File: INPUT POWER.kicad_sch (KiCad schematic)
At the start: 5 parts, among them J1 TYPE-C-31-M12_13

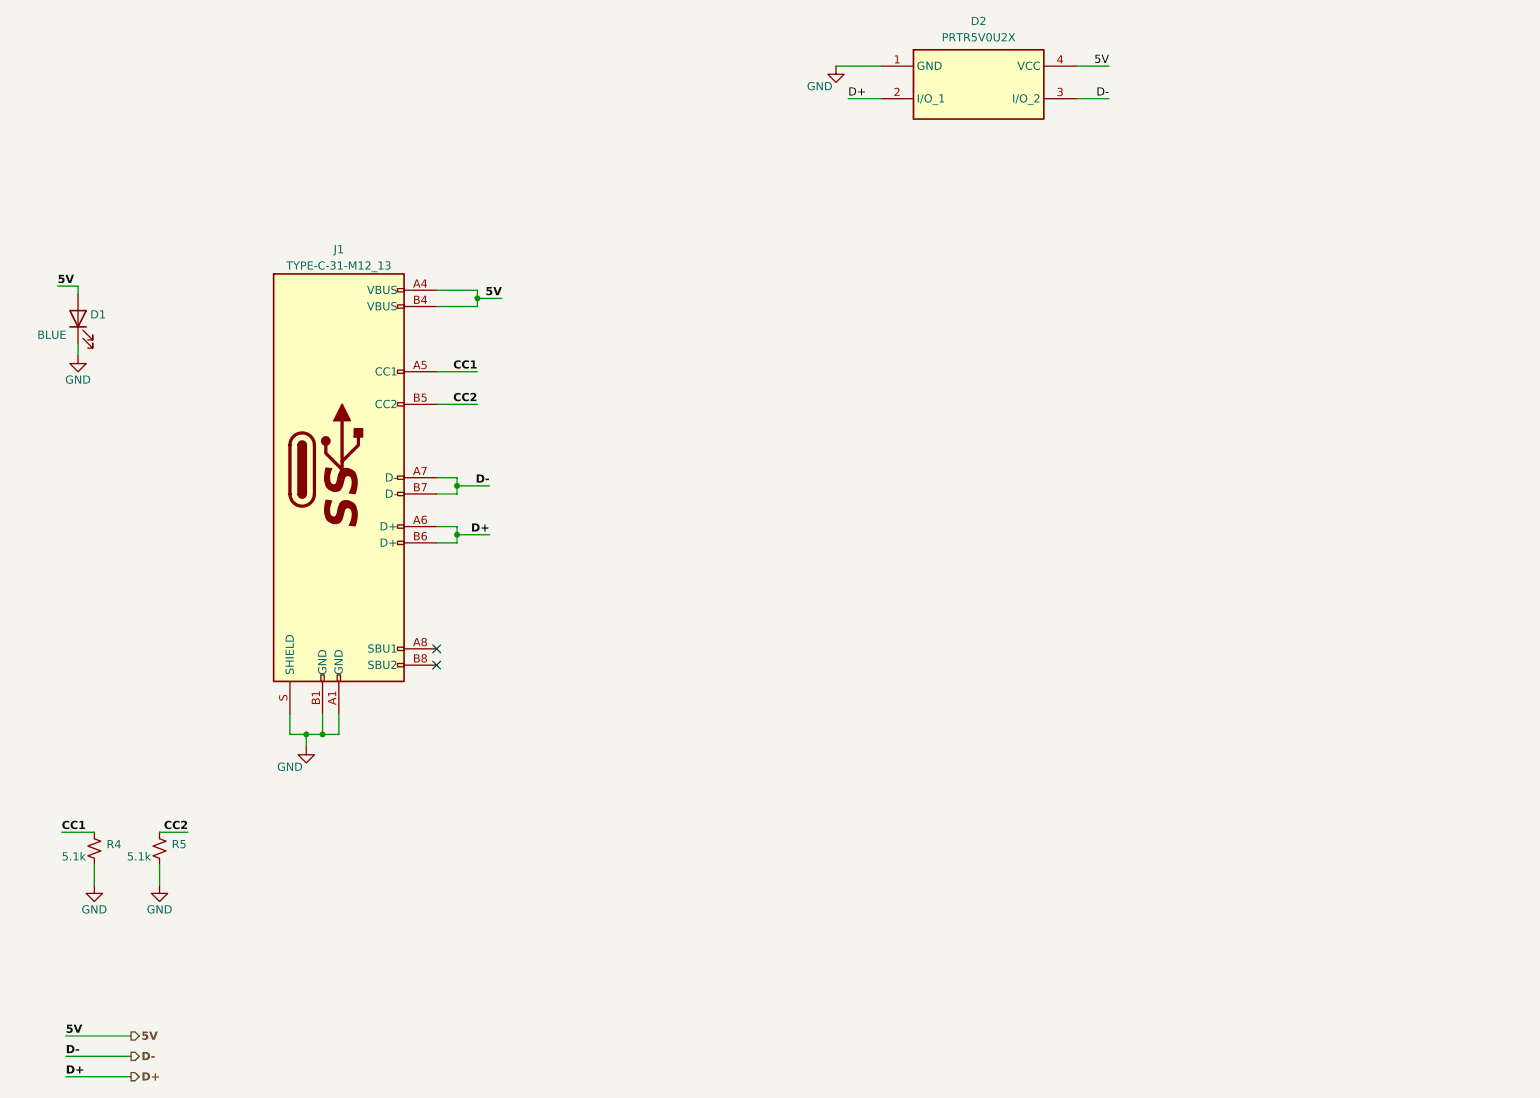
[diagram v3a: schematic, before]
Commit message: Added IP5306 for power path management
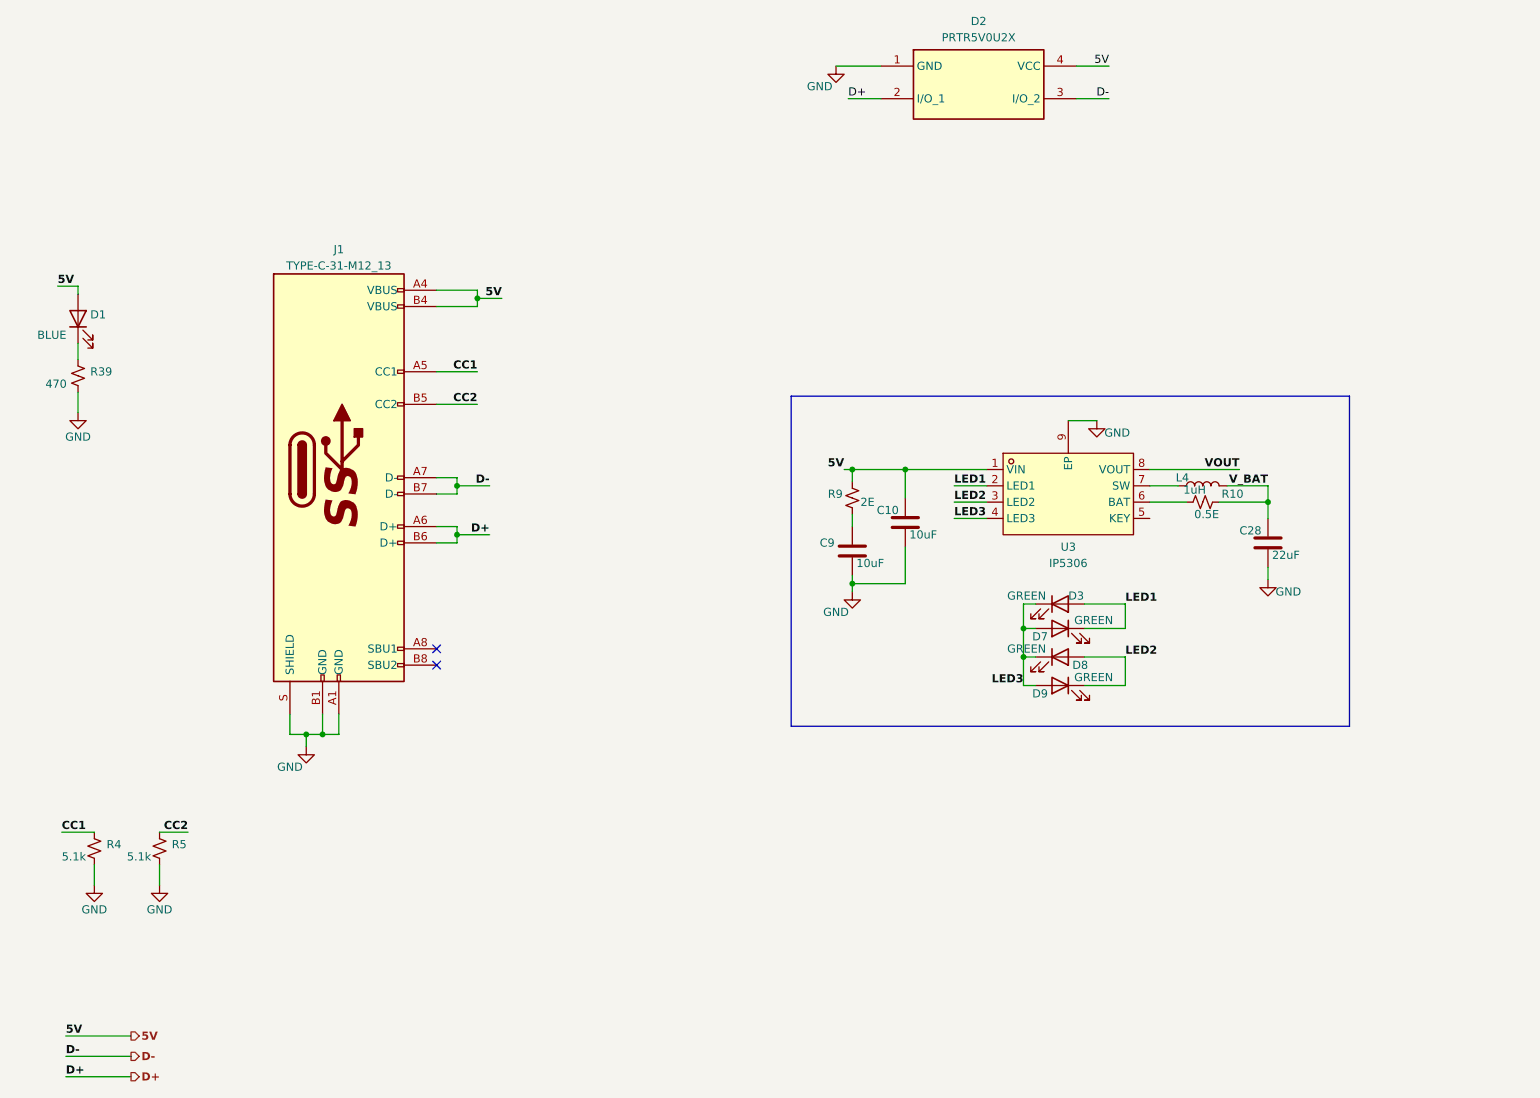
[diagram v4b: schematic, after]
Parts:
- added C10, C9: 10uF, symbol ESP32-S3_DB:C
- added C28: 22uF, symbol ESP32-S3_DB:C
- added D3, D7, D8, D9: GREEN, symbol ESP32-S3_DB:LED
- added L4: 1uH, symbol ESP32-S3_DB:L
- added R10: 0.5E, symbol ESP32-S3_DB:R_Small_US
- added R39: 470, symbol ESP32-S3_DB:R_Small_US
- added R9: 2E, symbol ESP32-S3_DB:R_Small_US
- added U3: IP5306, easyeda2kicad:ESOP-8_L4.9-W3.9-P1.27-LS6.0-BL-EP, symbol ESP32-S3_DB:IP5306
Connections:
- net 5V: now also C10.1, R9.1, U3.1 (VIN)
- net GND: now also C10.2, C28.2, C9.2, R39.2, U3.9 (EP); no longer D1.1 (K)
- new net: C9.1, R9.2
- new net: D1.1 (K), R39.1
- new net: R10.1, U3.6 (BAT)
- new net: L4.1, U3.7 (SW)
- new net LED1: D3.2 (A), D7.1 (K), U3.2 (LED1)
- new net LED2: D8.2 (A), D9.1 (K), U3.3 (LED2)
- new net LED3: D3.1 (K), D7.2 (A), D8.1 (K), D9.2 (A), U3.4 (LED3)
- new net VOUT: U3.8 (VOUT)
- new net V_BAT: C28.1, L4.2, R10.2

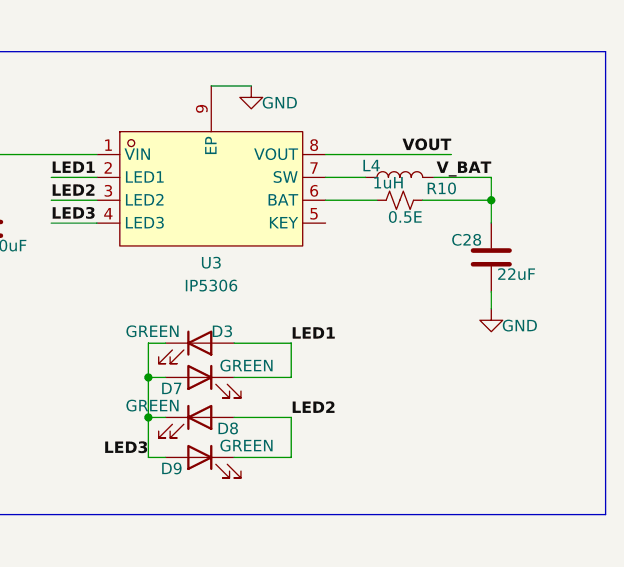
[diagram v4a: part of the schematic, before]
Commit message: Assigned UART port 2 for RS-485
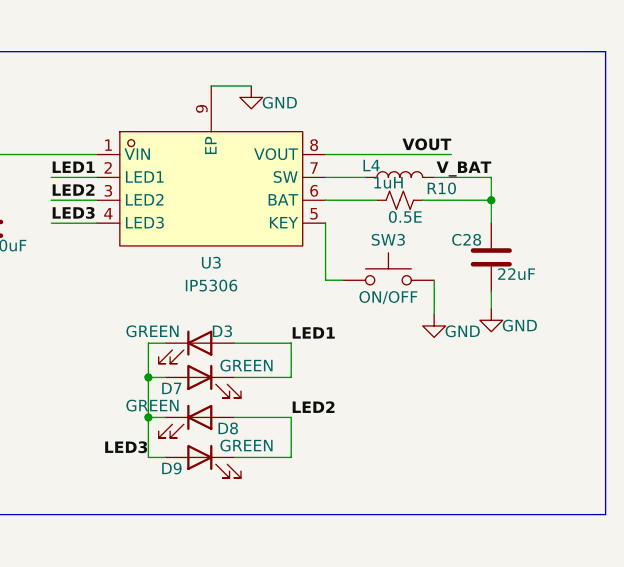
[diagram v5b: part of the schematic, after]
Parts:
- added SW3: ON/OFF, symbol ESP32-S3_DB:SW_Push
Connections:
- net GND: now also SW3.2
- net at U3.5 (KEY): now also SW3.1
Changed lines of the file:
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@@
+    (stroke (width 0) (type default))
+  )
+  (wire (pts (xy 205.105 111.76) (xy 205.105 107.95))
     (stroke (width 0) (type default))
   )
@@
   )
   (wire (pts (xy 173.355 114.935) (xy 173.355 118.745))
+    (stroke (width 0) (type default))
+  )
+  (wire (pts (xy 193.04 107.95) (xy 194.945 107.95))
     (stroke (width 0) (type default))
   )
@@
   )
   (wire (pts (xy 26.035 85.09) (xy 26.035 81.915))
+    (stroke (width 0) (type default))
+  )
+  (wire (pts (xy 193.04 101.6) (xy 193.04 107.95))
     (stroke (width 0) (type default))
   )
@@
         (path "/b7fc4bd3-c219-4455-832b-8d795385dcf1/95090a63-7b3c-4ea0-92b8-aeafe05264cd"
           (reference "R39") (unit 1)
+        )
+      )
+    )
+  )
+  (symbol (lib_id "ESP32-S3_DB:GND") (at 205.105 111.76 0) (unit 1)
+    (in_bom yes) (on_board yes) (dnp no)
+    (property "Reference" "#PWR053" (at 205.105 118.11 0)
+      (effects (font (size 1.27 1.27)) hide)
+    )
+    (property "Value" "GND" (at 208.28 113.665 0)
+      (effects (font (size 1.27 1.27)))
+    )
+    (property "Footprint" "" (at 205.105 111.76 0)
+      (effects (font (size 1.27 1.27)) hide)
+    )
+    (property "Datasheet" "" (at 205.105 111.76 0)
+      (effects (font (size 1.27 1.27)) hide)
+    )
+    (pin "1")
+    (instances
+      (project "ESP32-S3_DB"
+        (path "/b7fc4bd3-c219-4455-832b-8d795385dcf1/95090a63-7b3c-4ea0-92b8-aeafe05264cd"
+          (reference "#PWR053") (unit 1)
         )
       )
@@
         )
       )
+    )
+  )
+  (symbol (lib_id "ESP32-S3_DB:SW_Push") (at 200.025 107.95 0) (unit 1)
+    (in_bom yes) (on_board yes) (dnp no)
+    (property "Reference" "SW3" (at 200.025 103.505 0)
+      (effects (font (size 1.27 1.27)))
+    )
+    (property "Value" "ON/OFF" (at 200.025 109.855 0)
+      (effects (font (size 1.27 1.27)))
+    )
+    (property "Footprint" "" (at 200.025 102.87 0)
+      (effects (font (size 1.27 1.27)) hide)
+    )
+    (property "Datasheet" "~" (at 200.025 102.87 0)
+      (effects (font (size 1.27 1.27)) hide)
+    )
+    (pin "1")
+    (pin "2")
+    (instances
+      (project "ESP32-S3_DB"
+        (path "/b7fc4bd3-c219-4455-832b-8d795385dcf1/95090a63-7b3c-4ea0-92b8-aeafe05264cd"
+          (reference "SW3") (unit 1)
+        )
+      )

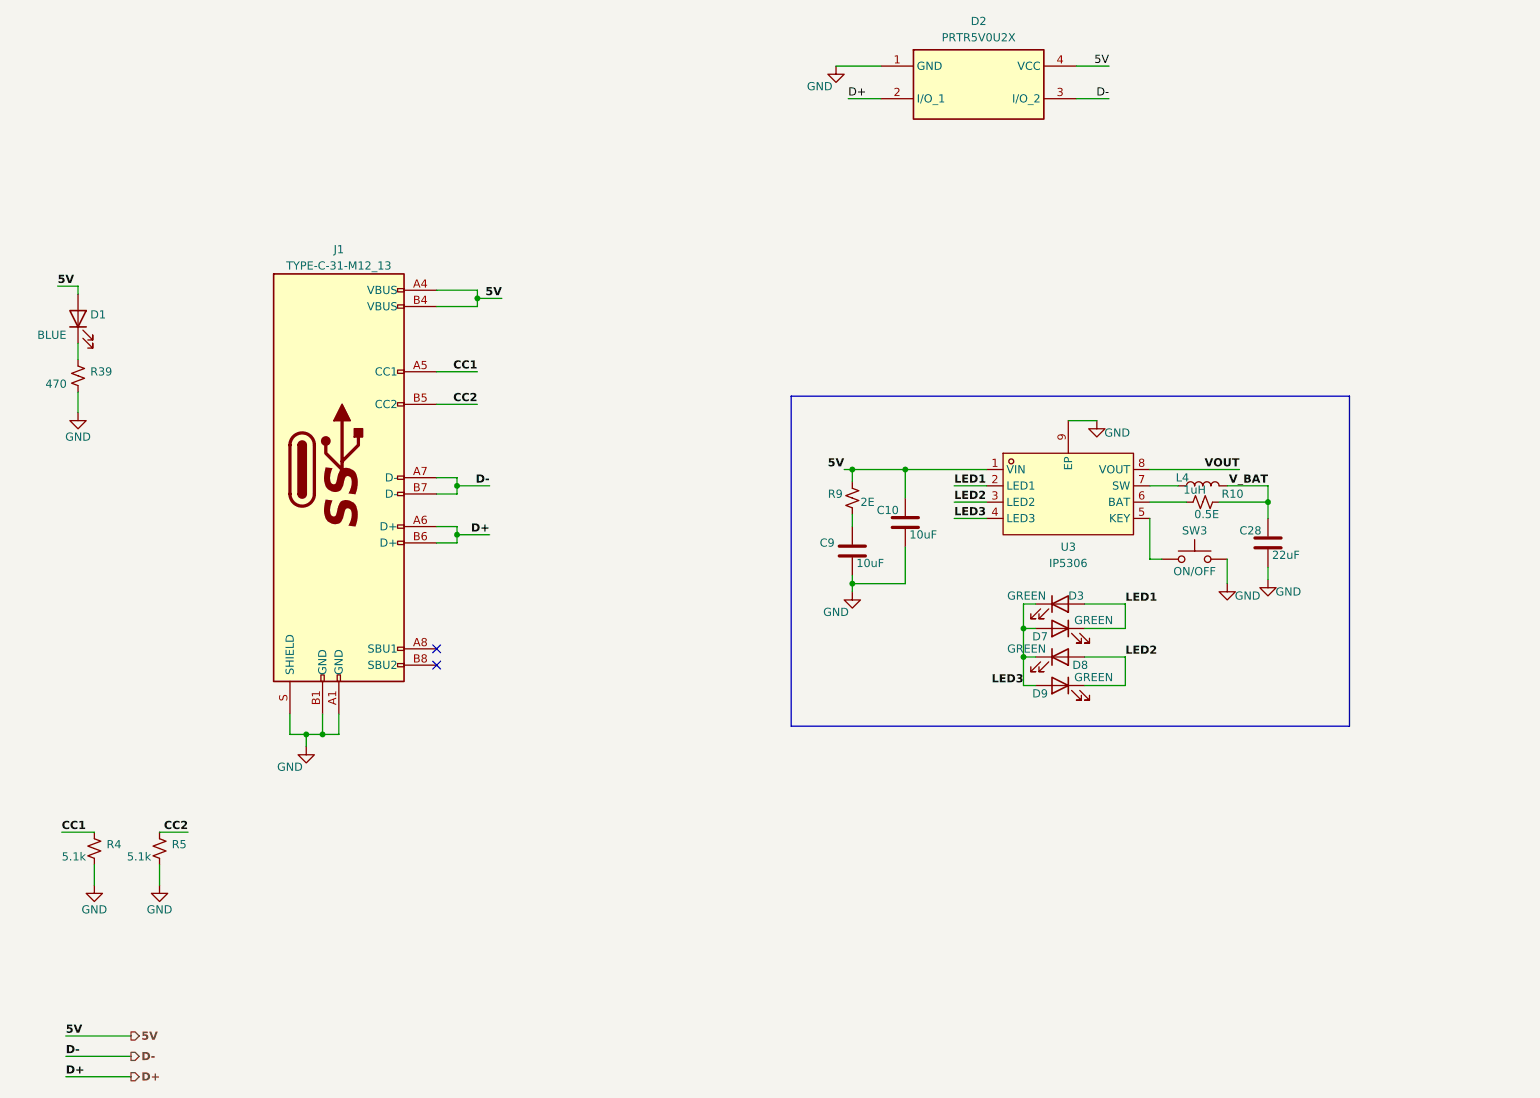
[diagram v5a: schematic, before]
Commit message: Added Female Headers
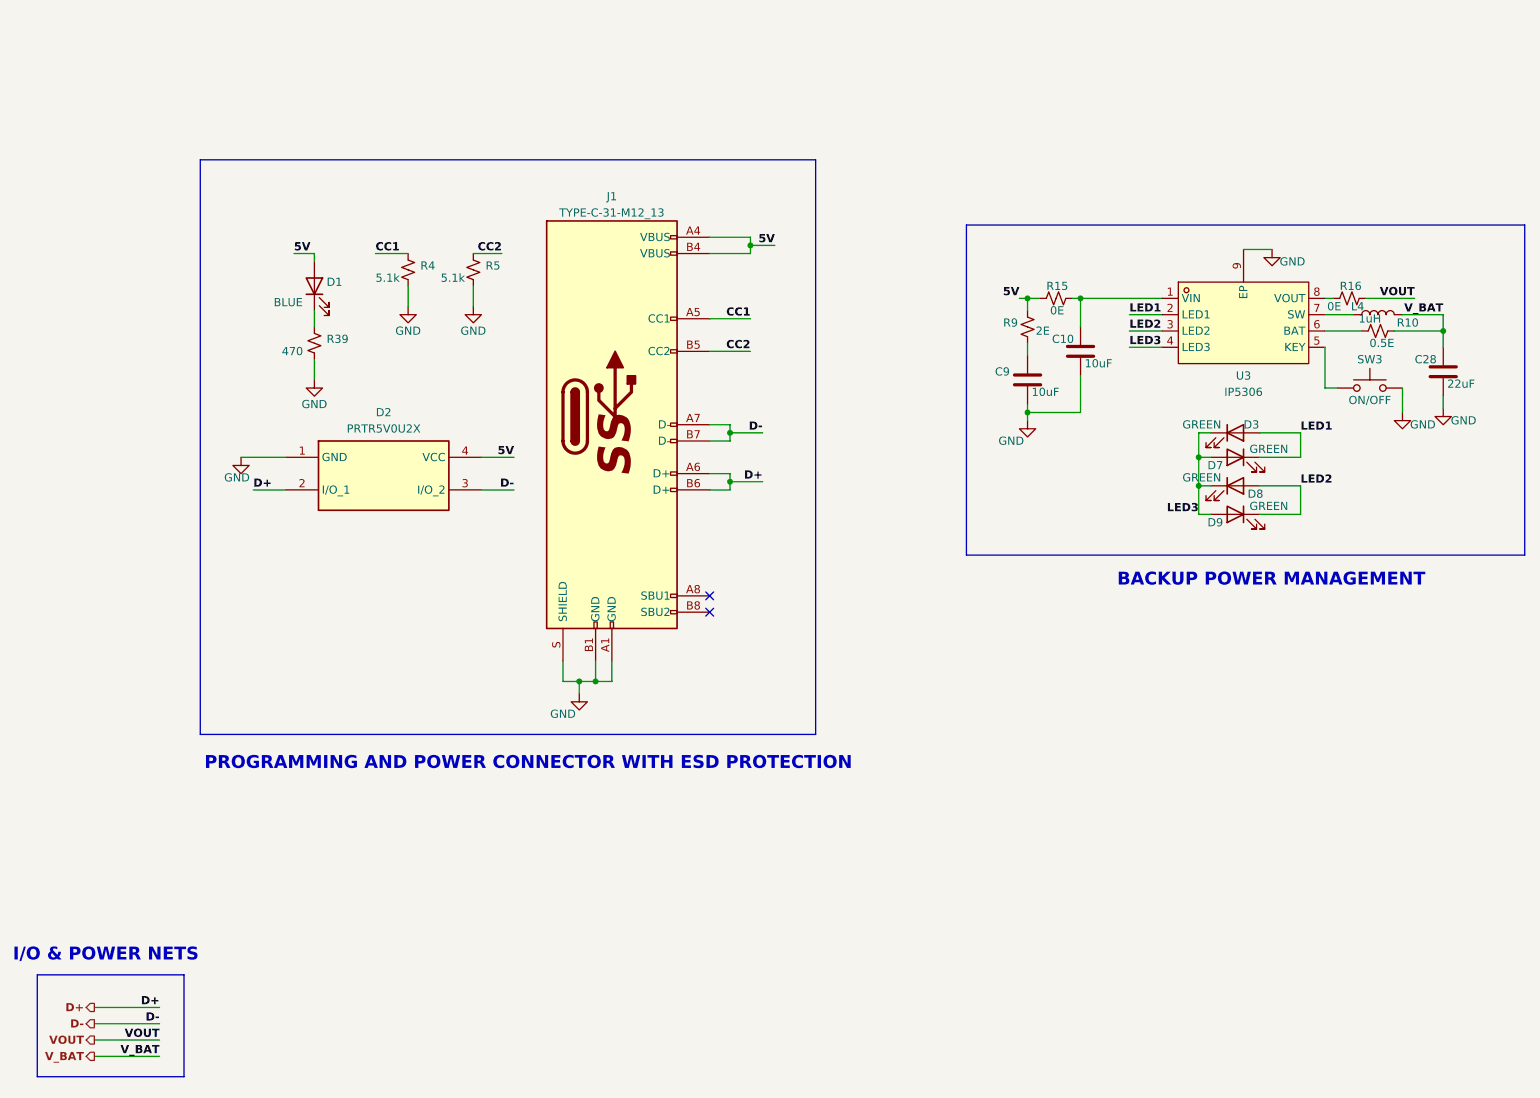
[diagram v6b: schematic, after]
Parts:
- added R15, R16: 0E, symbol ESP32-S3_DB:R_Small_US
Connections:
- net 5V: now also R15.1; no longer C10.1, U3.1 (VIN)
- net VOUT: now also R16.2; no longer U3.8 (VOUT)
- new net: R16.1, U3.8 (VOUT)
- new net: C10.1, R15.2, U3.1 (VIN)
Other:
- note added: "BACKUP POWER MANAGEMENT"
- note added: "I/O & POWER NETS"
- note added: "PROGRAMMING AND POWER CONNECTOR WITH ESD PROTECTION"
- moved on the sheet: C10, C28, C9, D1, D2, D3, D7, D8, D9, J1, L4, R10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
